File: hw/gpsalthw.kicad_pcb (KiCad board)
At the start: 2 copper layers, 91.2 x 50 mm, 61 parts, among them J2 display, J3 antenna, J4 USB_B_Micro, J5 battery, J6 A, J7 K, Q1 IRLML5203TRPBF, Q2 ML5203, Q3 S8050, Q4 s8050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

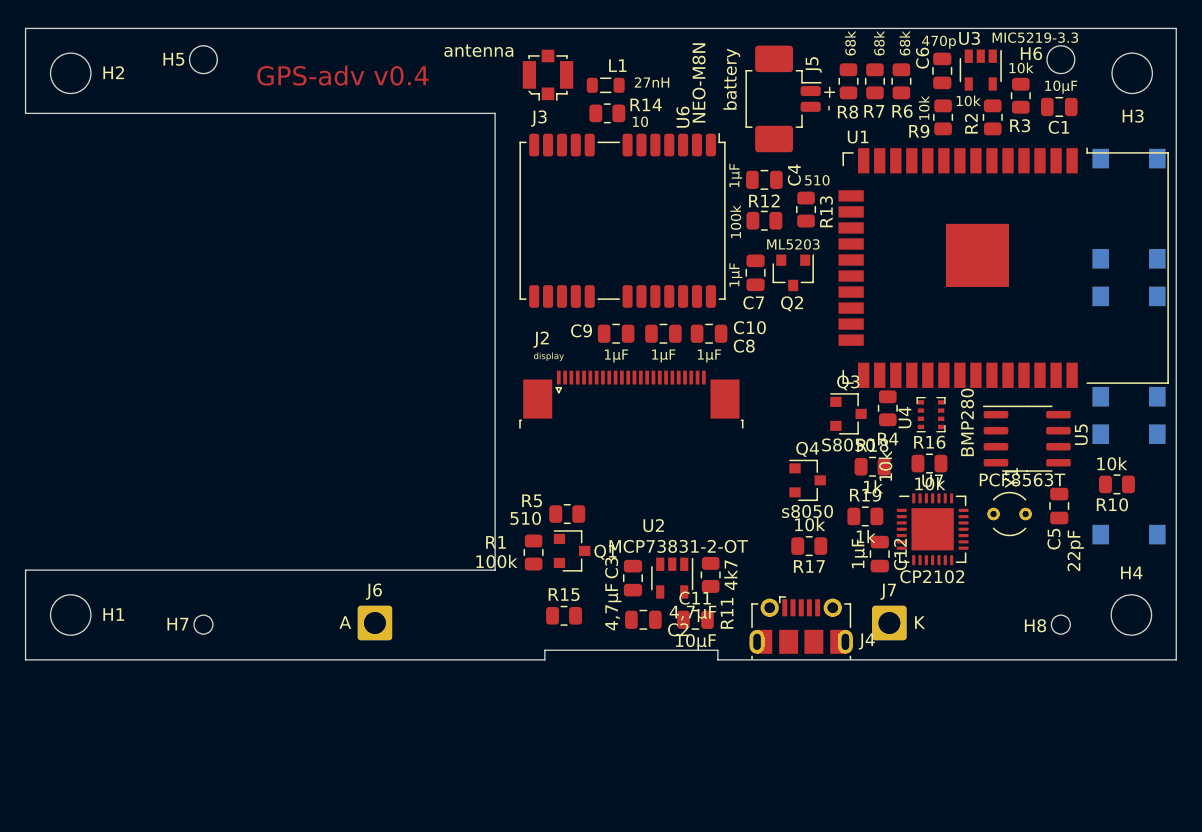
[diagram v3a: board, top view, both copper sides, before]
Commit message: плата - доработано крепление антенны
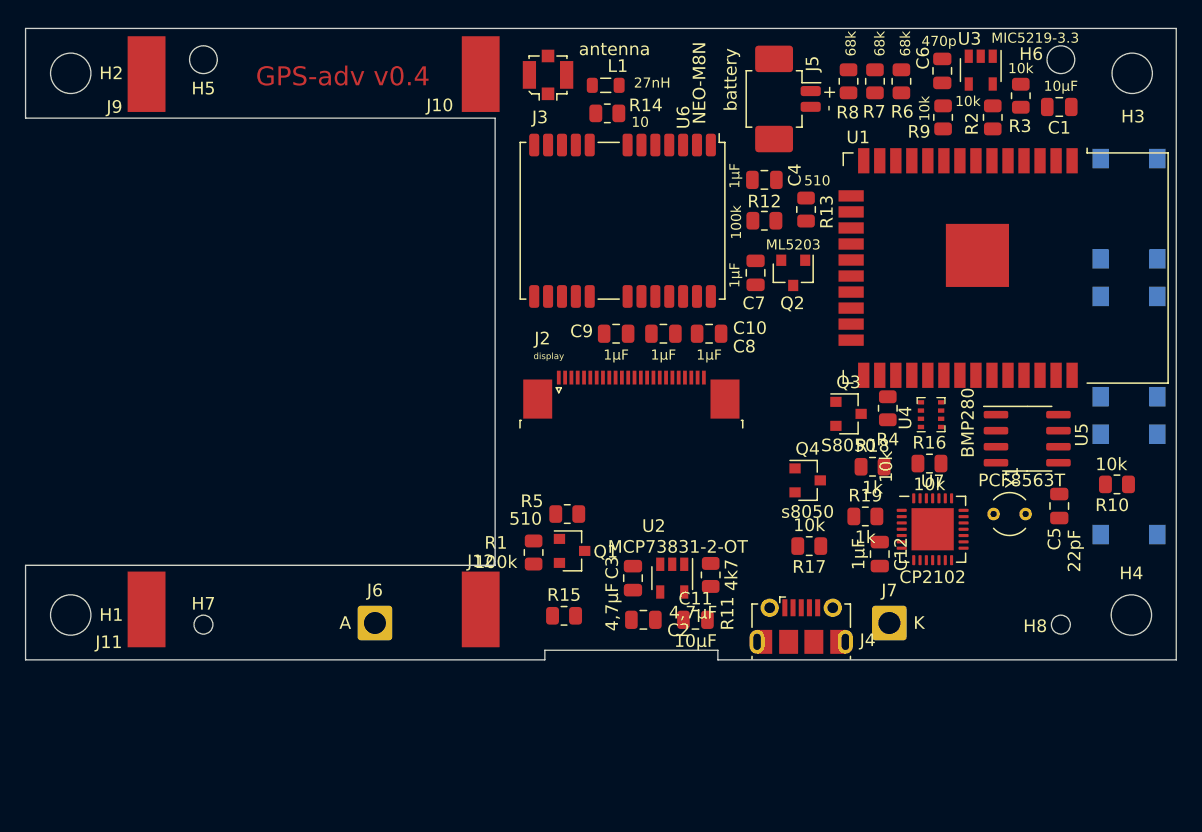
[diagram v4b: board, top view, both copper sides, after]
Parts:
- added J10: A, MHole:SolderWirePad_1x01_SMD_3x6mm, F.Cu at (80.9, 40.4)
- added J11: A, MHole:SolderWirePad_1x01_SMD_3x6mm, F.Cu at (54.4, 82.9)
- added J12: A, MHole:SolderWirePad_1x01_SMD_3x6mm, F.Cu at (80.9, 82.9)
- added J9: A, MHole:SolderWirePad_1x01_SMD_3x6mm, F.Cu at (54.4, 40.4)
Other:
- outline, holes or cut-outs redrawn
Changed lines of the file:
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@@
     (tracks 0)
     (zones 0)
-    (modules 61)
+    (modules 65)
     (nets 97)
   )
@@
     (add_net i2c-sda)
   )
+  (module MHole:SolderWirePad_1x01_SMD_3x6mm (layer F.Cu)
+    (at 80.899 82.8675)
+    (descr "Wire Pad, Square, SMD Pad,  3mm x 6mm,")
+    (tags "MesurementPoint Square SMDPad 3mmx6mm ")
+    (attr smd virtual)
+    (fp_text reference J12 (at 0 -3.81) (layer F.SilkS)
+      (effects (font (size 1 1) (thickness 0.15)))
+    )
+    (fp_text value A (at 0 6.35) (layer F.Fab) hide
+      (effects (font (size 1 1) (thickness 0.15)))
+    )
+    (fp_text user %R (at 0 0) (layer F.Fab)
+      (effects (font (size 1 1) (thickness 0.15)))
+    )
+    (fp_line (start 1.52 -3.05) (end -1.52 -3.05) (layer F.CrtYd) (width 0.05))
+    (fp_line (start 1.52 3.05) (end 1.52 -3.05) (layer F.CrtYd) (width 0.05))
+    (fp_line (start -1.52 3.05) (end 1.52 3.05) (layer F.CrtYd) (width 0.05))
+    (fp_line (start -1.52 -3.05) (end -1.52 3.05) (layer F.CrtYd) (width 0.05))
+    (pad 1 smd rect (at 0 0) (size 3 6) (layers F.Cu F.Paste F.Mask)
+      (net 1 GND))
+  )
+  (module MHole:SolderWirePad_1x01_SMD_3x6mm (layer F.Cu)
+    (at 54.4195 82.8675)
+    (descr "Wire Pad, Square, SMD Pad,  3mm x 6mm,")
+    (tags "MesurementPoint Square SMDPad 3mmx6mm ")
+    (attr smd virtual)
+    (fp_text reference J11 (at -2.9845 2.6035) (layer F.SilkS)
+      (effects (font (size 1 1) (thickness 0.15)))
+    )
+    (fp_text value A (at 0 6.35) (layer F.Fab) hide
+      (effects (font (size 1 1) (thickness 0.15)))
+    )
+    (fp_text user %R (at 0 0) (layer F.Fab)
+      (effects (font (size 1 1) (thickness 0.15)))
+    )
+    (fp_line (start 1.52 -3.05) (end -1.52 -3.05) (layer F.CrtYd) (width 0.05))
+    (fp_line (start 1.52 3.05) (end 1.52 -3.05) (layer F.CrtYd) (width 0.05))
+    (fp_line (start -1.52 3.05) (end 1.52 3.05) (layer F.CrtYd) (width 0.05))
+    (fp_line (start -1.52 -3.05) (end -1.52 3.05) (layer F.CrtYd) (width 0.05))
+    (pad 1 smd rect (at 0 0) (size 3 6) (layers F.Cu F.Paste F.Mask)
+      (net 1 GND))
+  )
+  (module MHole:SolderWirePad_1x01_SMD_3x6mm (layer F.Cu)
+    (at 80.899 40.4495)
+    (descr "Wire Pad, Square, SMD Pad,  3mm x 6mm,")
+    (tags "MesurementPoint Square SMDPad 3mmx6mm ")
+    (attr smd virtual)
+    (fp_text reference J10 (at -3.2385 2.4765) (layer F.SilkS)
+      (effects (font (size 1 1) (thickness 0.15)))
+    )
+    (fp_text value A (at 0 6.35) (layer F.Fab) hide
+      (effects (font (size 1 1) (thickness 0.15)))
+    )
+    (fp_text user %R (at 0 0) (layer F.Fab)
+      (effects (font (size 1 1) (thickness 0.15)))
+    )
+    (fp_line (start 1.52 -3.05) (end -1.52 -3.05) (layer F.CrtYd) (width 0.05))
+    (fp_line (start 1.52 3.05) (end 1.52 -3.05) (layer F.CrtYd) (width 0.05))
+    (fp_line (start -1.52 3.05) (end 1.52 3.05) (layer F.CrtYd) (width 0.05))
+    (fp_line (start -1.52 -3.05) (end -1.52 3.05) (layer F.CrtYd) (width 0.05))
+    (pad 1 smd rect (at 0 0) (size 3 6) (layers F.Cu F.Paste F.Mask)
+      (net 1 GND))
+  )
+  (module MHole:SolderWirePad_1x01_SMD_3x6mm (layer F.Cu)
+    (at 54.4195 40.4495)
+    (descr "Wire Pad, Square, SMD Pad,  3mm x 6mm,")
+    (tags "MesurementPoint Square SMDPad 3mmx6mm ")
+    (attr smd virtual)
+    (fp_text reference J9 (at -2.54 2.6035) (layer F.SilkS)
+      (effects (font (size 1 1) (thickness 0.15)))
+    )
+    (fp_text value A (at 0 6.35) (layer F.Fab) hide
+      (effects (font (size 1 1) (thickness 0.15)))
+    )
+    (fp_text user %R (at 0 0) (layer F.Fab)
+      (effects (font (size 1 1) (thickness 0.15)))
+    )
+    (fp_line (start 1.52 -3.05) (end -1.52 -3.05) (layer F.CrtYd) (width 0.05))
+    (fp_line (start 1.52 3.05) (end 1.52 -3.05) (layer F.CrtYd) (width 0.05))
+    (fp_line (start -1.52 3.05) (end 1.52 3.05) (layer F.CrtYd) (width 0.05))
+    (fp_line (start -1.52 -3.05) (end -1.52 3.05) (layer F.CrtYd) (width 0.05))
+    (pad 1 smd rect (at 0 0) (size 3 6) (layers F.Cu F.Paste F.Mask)
+      (net 1 GND))
+  )
   (module Connector_Wire:SolderWire-1sqmm_1x01_D1.4mm_OD2.7mm (layer F.Cu)
     (at 113.284 83.947)
@@
     (tags "mounting hole 2.2mm no annular m2")
     (attr virtual)
-    (fp_text reference H5 (at -2.3495 0) (layer F.SilkS)
+    (fp_text reference H5 (at 0 2.286) (layer F.SilkS)
       (effects (font (size 1 1) (thickness 0.15)))
     )
@@
     (tags "mounting hole 1.5mm no annular")
     (attr virtual)
-    (fp_text reference H7 (at -2.032 0) (layer F.SilkS)
+    (fp_text reference H7 (at 0 -1.651) (layer F.SilkS)
       (effects (font (size 1 1) (thickness 0.15)))
     )
@@
       (effects (font (size 1 1) (thickness 0.15)))
     )
-    (fp_text value antenna (at -5.461 -1.905 180) (layer F.SilkS)
+    (fp_text value antenna (at 5.2705 -2.032 180) (layer F.SilkS)
       (effects (font (size 1 1) (thickness 0.15)))
     )
@@
     (tags "mounting hole 3.2mm no annular m3")
     (attr virtual)
-    (fp_text reference H2 (at 3.404 0) (layer F.SilkS)
+    (fp_text reference H2 (at 3.2135 0) (layer F.SilkS)
       (effects (font (size 1 1) (thickness 0.15)))
     )
@@
     (tags "mounting hole 3.2mm no annular m3")
     (attr virtual)
-    (fp_text reference H1 (at 3.404 0) (layer F.SilkS)
+    (fp_text reference H1 (at 3.2135 0) (layer F.SilkS)
       (effects (font (size 1 1) (thickness 0.15)))
     )
@@
   (gr_line (start 85.979 86.868) (end 85.979 86.106) (layer Edge.Cuts) (width 0.05))
   (gr_line (start 99.695 86.868) (end 99.695 86.106) (layer Edge.Cuts) (width 0.05))
-  (gr_line (start 44.831 43.561) (end 44.831 36.83) (layer Edge.Cuts) (width 0.05))
-  (gr_line (start 44.831 79.756) (end 44.831 86.868) (layer Edge.Cuts) (width 0.05))
-  (gr_line (start 82.042 79.756) (end 44.831 79.756) (layer Edge.Cuts) (width 0.05))
-  (gr_line (start 82.042 43.561) (end 82.042 79.756) (layer Edge.Cuts) (width 0.05))
-  (gr_line (start 44.831 43.561) (end 82.042 43.561) (layer Edge.Cuts) (width 0.05))
+  (gr_line (start 44.831 43.942) (end 44.831 36.83) (layer Edge.Cuts) (width 0.05))
+  (gr_line (start 44.831 79.375) (end 44.831 86.868) (layer Edge.Cuts) (width 0.05))
+  (gr_line (start 82.042 79.375) (end 44.831 79.375) (layer Edge.Cuts) (width 0.05))
+  (gr_line (start 82.042 43.942) (end 82.042 79.375) (layer Edge.Cuts) (width 0.05))
+  (gr_line (start 44.831 43.942) (end 82.042 43.942) (layer Edge.Cuts) (width 0.05))
   (gr_circle (center 72.603986 84.050514) (end 73.111986 84.495014) (layer Dwgs.User) (width 0.15))
   (gr_circle (center 113.116986 84.050514) (end 113.624986 84.495014) (layer Dwgs.User) (width 0.15))

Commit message: плата - дораскиданы элементы, можно трассировать
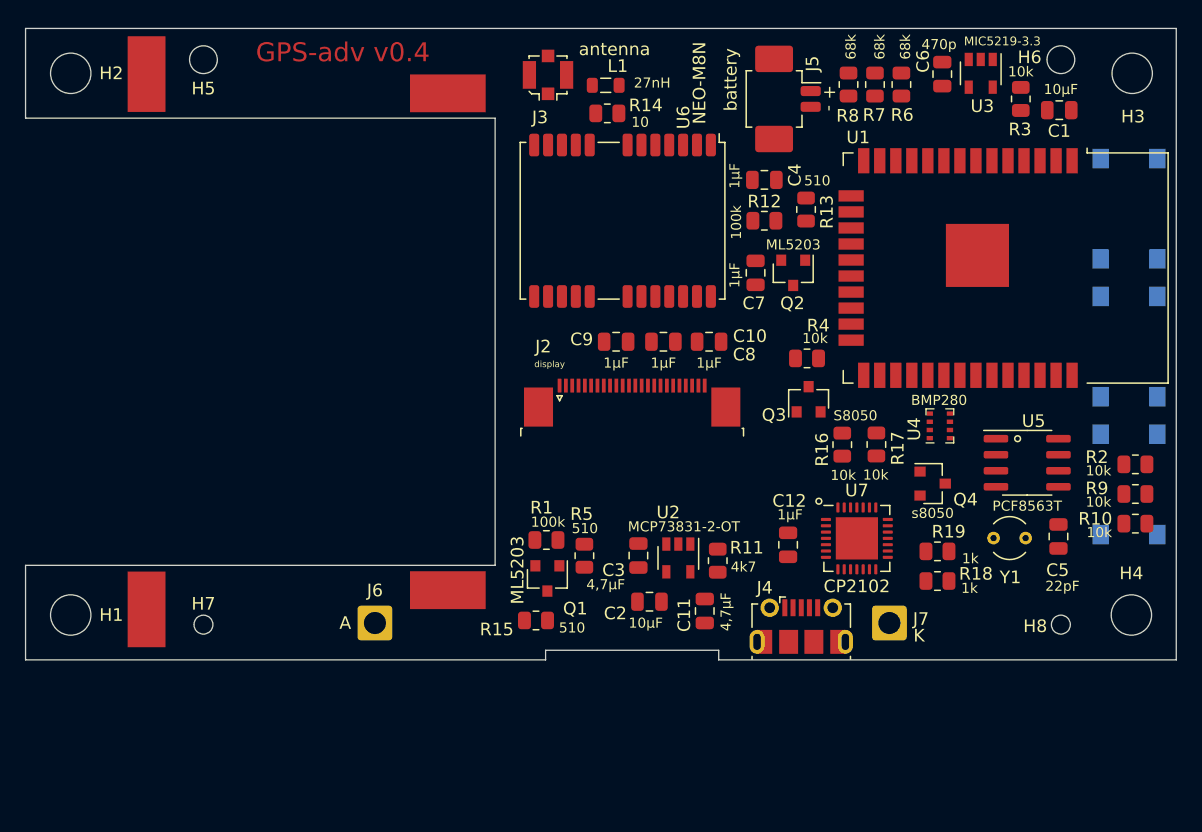
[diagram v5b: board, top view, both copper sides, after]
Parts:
- Q1: value IRLML5203TRPBF -> ML5203
- moved R9 33.5 mm to (132.8, 73.7), turned to 0 degrees
- moved R2 29.7 mm to (132.8, 71.4), turned to 0 degrees
- moved R18 10.4 mm to (117.1, 80.6)
- moved Q4 9.91 mm to (116.7, 72.9)
- moved R17 9.65 mm to (112.3, 69.8), turned to 270 degrees
- moved R4 7.52 mm to (106.8, 63.0), turned to 0 degrees
- moved C12 7.30 mm to (105.3, 77.7)
- moved R16 7.07 mm to (109.6, 69.8), turned to 270 degrees
- moved R19 6.35 mm to (117.1, 78.3)
- moved U7 6.05 mm to (110.7, 77.2)
- moved R5 3.57 mm to (89.1, 78.6), turned to 270 degrees
- moved R10 3.44 mm to (132.8, 76.1), turned to 0 degrees
- moved Q3 3.37 mm to (106.9, 66.2), turned to 90 degrees
- moved J10 3.02 mm to (78.3, 42.0), turned to 90 degrees
- moved J12 3.02 mm to (78.3, 81.3), turned to 90 degrees
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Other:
- outline, holes or cut-outs redrawn

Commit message: плата - растрассирована, теперь гербер
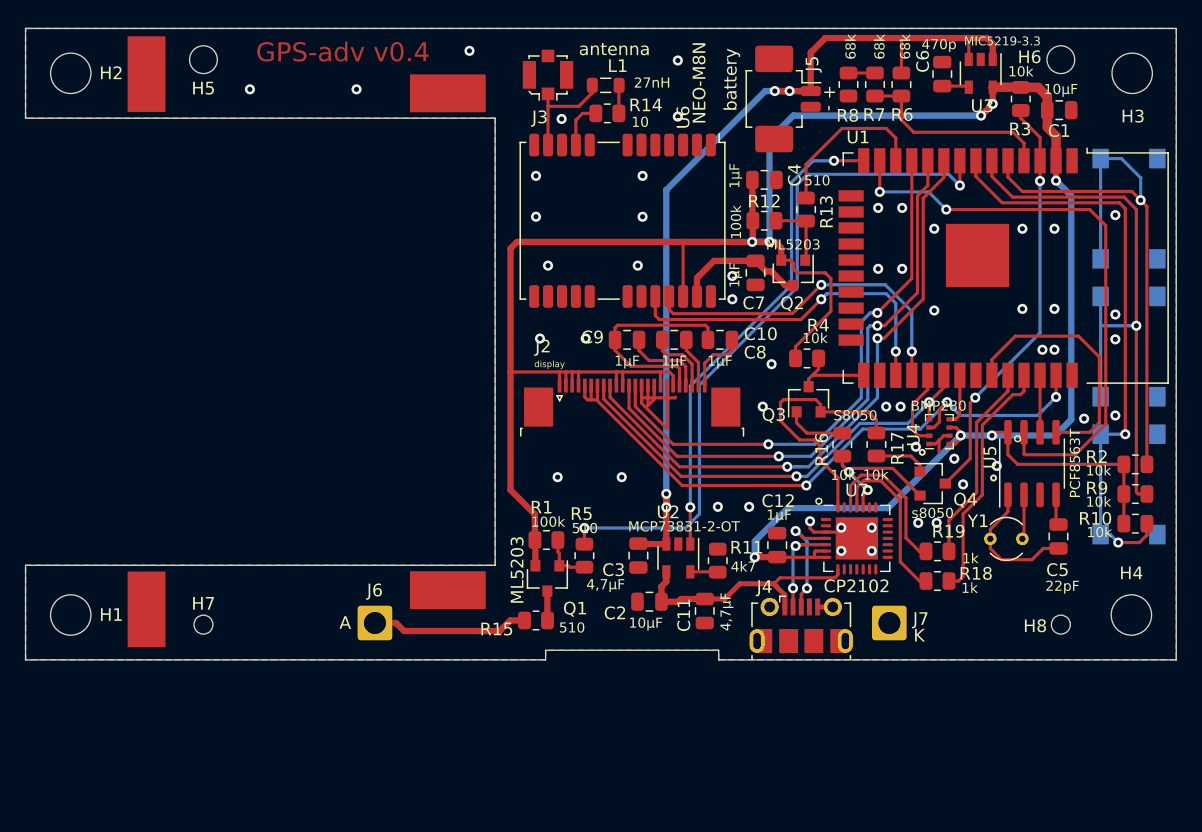
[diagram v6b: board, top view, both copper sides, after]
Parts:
- moved Y1 2.79 mm to (121.3, 77.3), turned to 0 degrees
- moved C10 0.88 mm to (96.2, 61.5)
- moved C8 0.88 mm to (99.9, 61.5)
- moved C9 0.88 mm to (92.5, 61.5)
- moved C12 0.86 mm to (104.4, 77.8)
- moved U4 0.46 mm to (117.2, 68.8)
- moved U5 0.39 mm to (124.6, 71.3), turned to 90 degrees
- moved J4 0.06 mm to (106.3, 84.1)
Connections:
- J2 pad MP: (no net) -> GND
- U1 pad 10: /d-rst -> /d-rs-dc
- U1 pad 9: /d-rs-dc -> /d-rst
- U5 pad 3: clk-int -> Net-(U5-Pad3)
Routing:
- net +3V3: track 0.00 -> 211.1 mm, vias 0 -> 8
- net +BATT: track 0.00 -> 71.1 mm, vias 0 -> 4
- net d-led: track 0.00 -> 55.7 mm, vias 0 -> 2
- net /spi-mosi: track 0.00 -> 51.8 mm, vias 0 -> 3
- net /d-rst: track 0.00 -> 49.1 mm, vias 0 -> 2
- net /b-sel: track 0.00 -> 47.9 mm, vias 0 -> 1
- net /b-up: track 0.00 -> 47.2 mm, vias 0 -> 1
- net /b-down: track 0.00 -> 47.0 mm, vias 0 -> 2
- net clk-int: track 0.00 -> 46.4 mm, vias 0 -> 2
- net /d-rs-dc: track 0.00 -> 45.7 mm, vias 0 -> 2
- net /d-cs: track 0.00 -> 43.1 mm, vias 0 -> 2
- net chg-ind: track 0.00 -> 38.4 mm, vias 0 -> 2
- net /spi-clk: track 0.00 -> 35.8 mm, vias 0 -> 2
- net /s-en: track 0.00 -> 33.3 mm, vias 0 -> 2
- net /gps-tx: track 0.00 -> 27.6 mm, vias 0 -> 2
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- added copper zone on B.Cu, net GND
- added copper zone on F.Cu, net GND

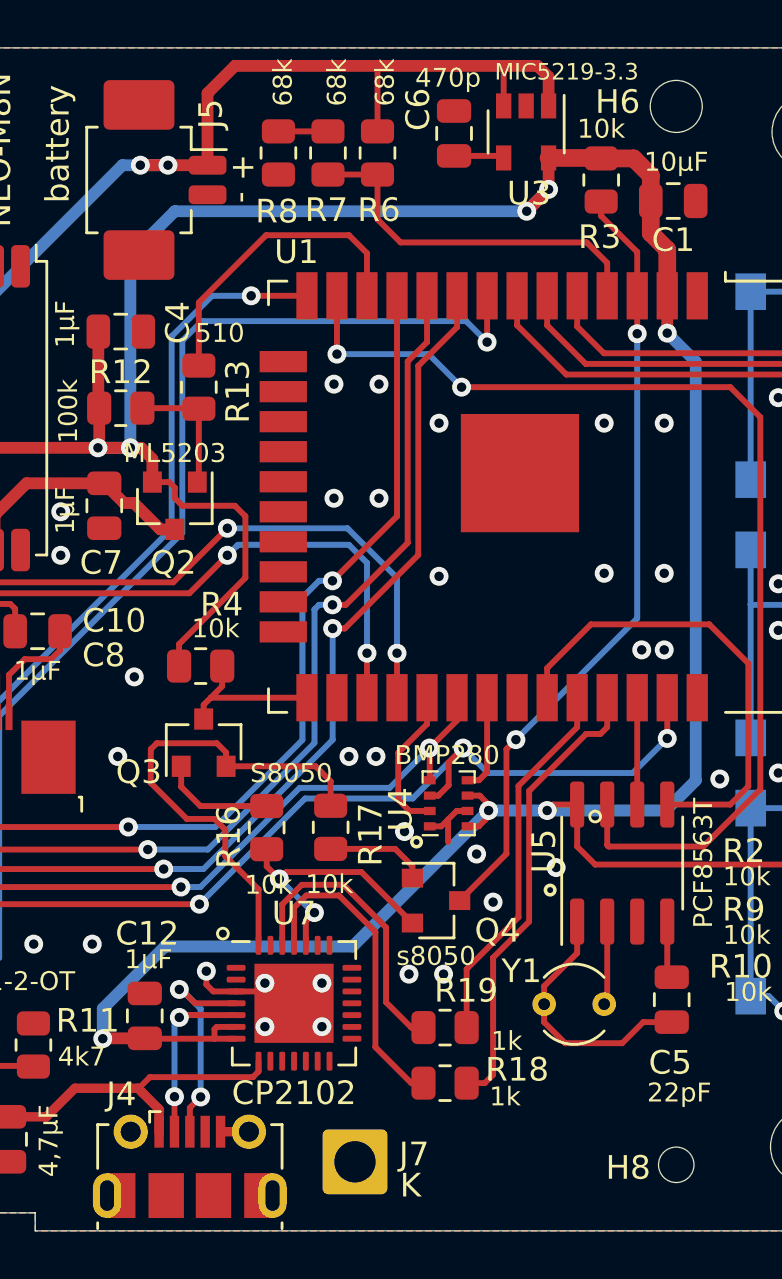
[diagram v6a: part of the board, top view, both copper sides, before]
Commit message: плата - исправлены проблемы подключения uart
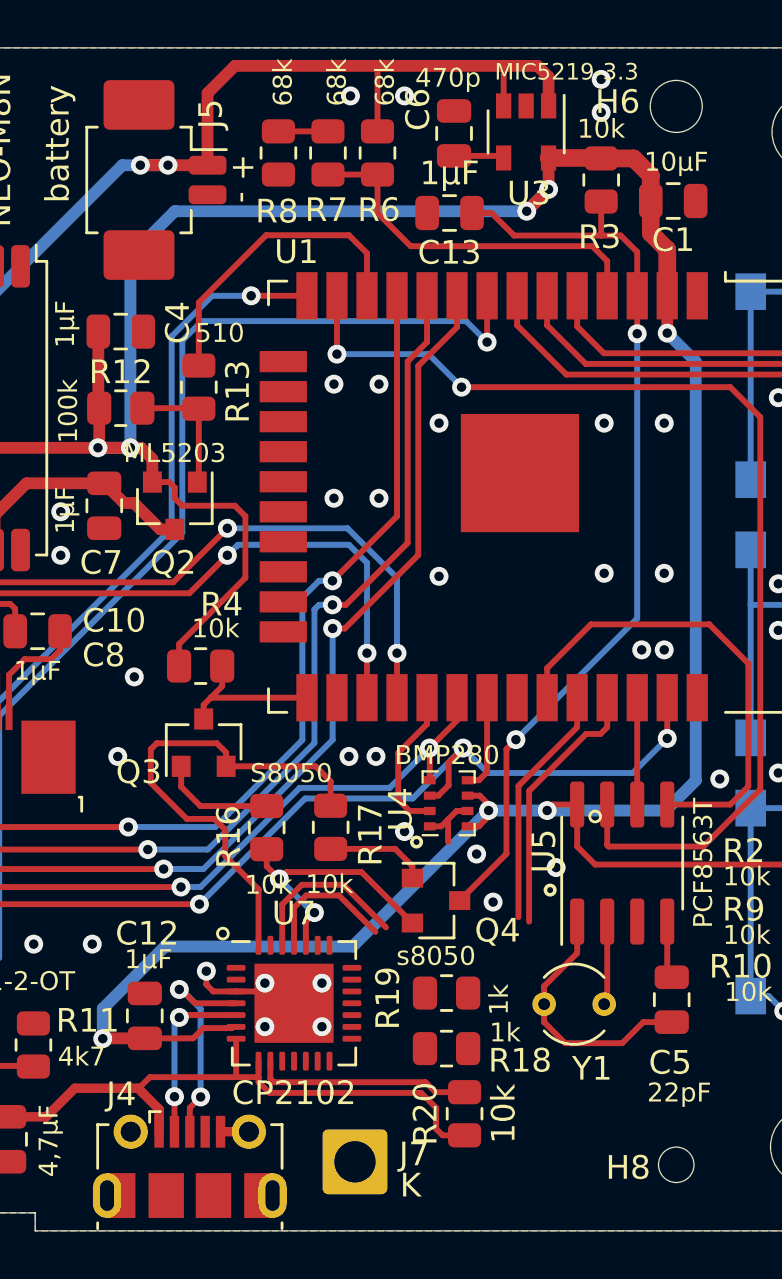
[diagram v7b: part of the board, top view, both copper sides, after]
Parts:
- added C13: 1μF, Capacitor_SMD:C_0805_2012Metric, F.Cu at (117.3, 43.8)
- added R20: 10k, Resistor_SMD:R_0805_2012Metric, F.Cu at (117.9, 81.9)
- moved R18 1.46 mm to (117.2, 79.2)
- moved R19 1.46 mm to (117.2, 76.8)
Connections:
- U7 pad 7: +3V3 -> /usb-5v
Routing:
- net /usb-5v: track 20.1 -> 32.3 mm
- net Net-(R20-Pad2): track 0.00 -> 9.19 mm
- net /s-tx: track 19.6 -> 11.2 mm
- net Net-(R18-Pad1): track 13.4 -> 5.89 mm
- net /s-en: track 33.3 -> 39.7 mm
- net /s-rx: track 15.9 -> 10.3 mm
- net Net-(R19-Pad1): track 12.4 -> 7.21 mm
- net +3V3: track 211.1 -> 209.9 mm
- net GND: vias 52 -> 54
